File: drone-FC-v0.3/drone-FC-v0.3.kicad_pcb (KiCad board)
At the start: 2 copper layers, 68 parts, among them J1 USB_C_Receptacle_USB2.0_16P, J10 M1, J11 USB_C_Receptacle_USB2.0_16P, J2 Conn_01x04_Pin, J3 S2, J4 S3, J5 S1, J6 Conn_01x04_Pin, J7 ICM, J8 UART0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

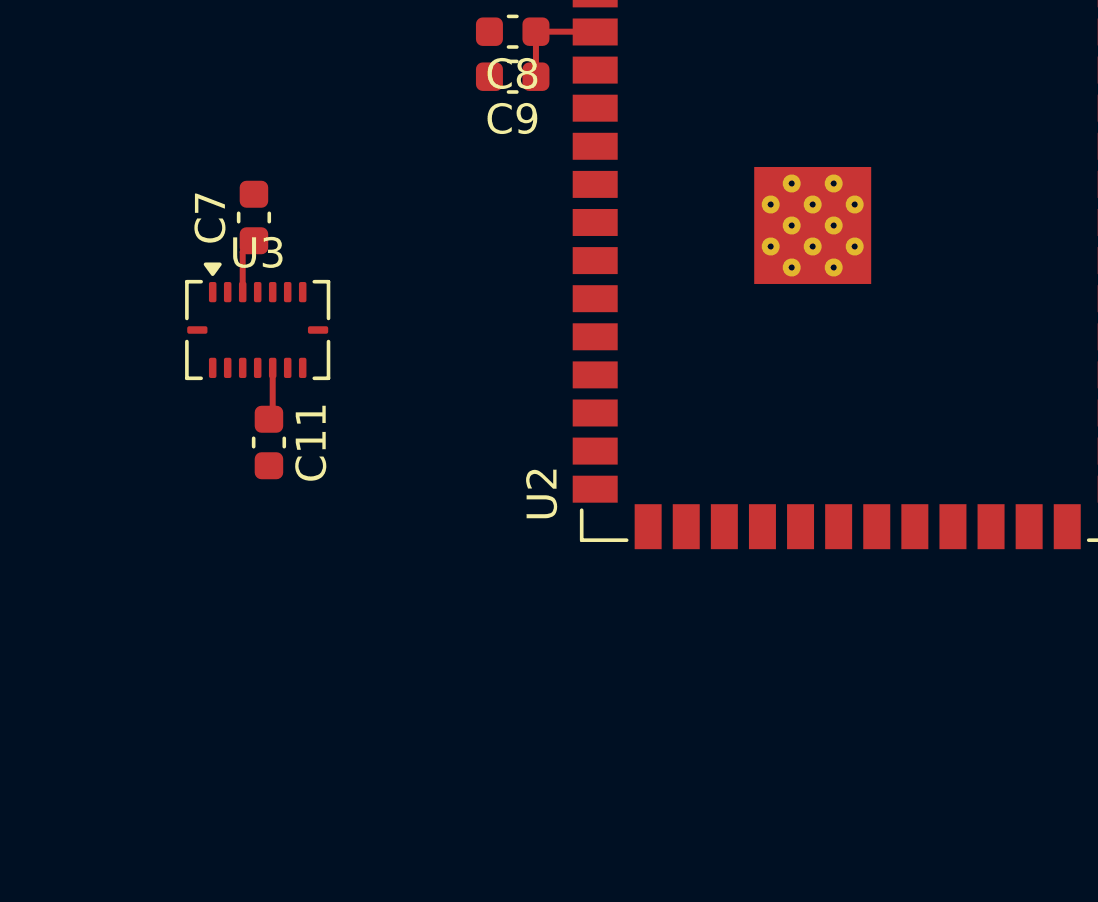
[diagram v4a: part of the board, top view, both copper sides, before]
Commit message: connected U3 to U2
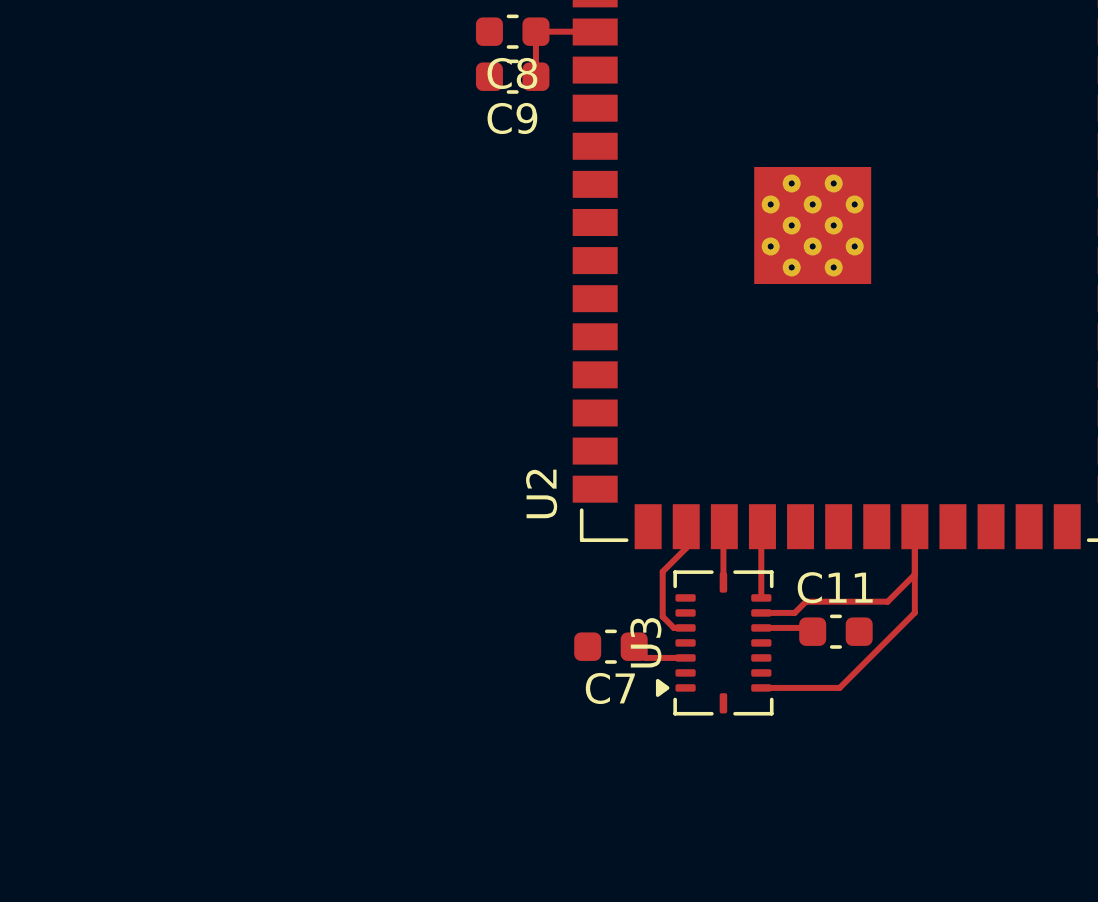
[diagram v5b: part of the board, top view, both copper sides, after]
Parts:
- moved C11 19.9 mm to (137.3, 72.0), turned to 0 degrees
- moved U3 18.7 mm to (133.5, 72.4), turned to 90 degrees
- moved C7 18.6 mm to (129.8, 72.5), turned to 180 degrees
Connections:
- net /Sensors/INT1_ACCEL renamed GPIO4
- net /Sensors/INT2_ACCEL renamed GPIO5
- net /Sensors/INT3_GYRO renamed GPIO6
- net /Sensors/INT4_GYRO renamed GPIO7
- D7 pad 2: /MCU/GPIO 19 -> USB_D-
- D9 pad 2: /MCU/GPIO 20 -> USB_D+
- J10 pad 1: /Power/GPIO8 -> GPIO 8
- J11 pad A6: /MCU/GPIO 20 -> USB_D+
- J11 pad A7: /MCU/GPIO 19 -> USB_D-
- J11 pad B6: /MCU/GPIO 20 -> USB_D+
- J11 pad B7: /MCU/GPIO 19 -> USB_D-
- J2 pad 3: /Sensors/SDA_MAG -> SDA_MAG
- J2 pad 4: /Sensors/SCL_MAG -> SCL_MAG
- J3 pad 1: /Power/GPIO5 -> GPIO 5
- J4 pad 1: /Power/GPIO6 -> GPIO 6
- J5 pad 1: /Power/GPIO4 -> GPIO 4
- J9 pad 1: /Power/GPIO7 -> GPIO 7
- R10 pad 2: /Sensors/SCLK -> SCLK
- R7 pad 2: /Sensors/SCL_MAG -> SCL_MAG
- R8 pad 2: /Sensors/SDA_MAG -> SDA_MAG
- R9 pad 2: /Sensors/GPIO8 -> GPIO 8
- U2 pad 12: /MCU/GPIO8 -> GPIO 8
- U2 pad 13: /MCU/USB_D- -> USB_D-
- U2 pad 14: /MCU/USB_D+ -> USB_D+
- U2 pad 15: /MCU/SCLK -> unconnected-(U2-IO3-Pad15)
- U2 pad 16: unconnected-(U2-IO46-Pad16) -> CSB_GYRO
- U2 pad 17: /MCU/Low_chip_selected -> SCLK
- U2 pad 18: /MCU/SCL_MAG -> MOSI
- U2 pad 19: /MCU/SDA_MAG -> unconnected-(U2-IO11-Pad19)
- U2 pad 20: unconnected-(U2-IO12-Pad20) -> SCL_MAG
- U2 pad 21: unconnected-(U2-IO13-Pad21) -> SDA_MAG
- U2 pad 22: unconnected-(U2-IO14-Pad22) -> MISO
- U2 pad 30: /MCU/SDO1 -> SDO1
- U2 pad 4: /MCU/GPIO4 -> GPIO 4
- U2 pad 5: /MCU/GPIO5 -> GPIO 5
- U2 pad 6: /MCU/GPIO6 -> GPIO 6
- U2 pad 7: /MCU/GPIO7 -> GPIO 7
- U2 pad 8: unconnected-(U2-IO15-Pad8) -> GPIO15
- U3 pad 10: /Sensors/MISO -> MISO
- U3 pad 14: /Sensors/CSB_ACCEL -> GPIO15
- U3 pad 15: /Sensors/MISO -> MISO
- U3 pad 5: /Sensors/CSB_GYRO -> CSB_GYRO
- U3 pad 8: /Sensors/SCK -> SCLK
- U3 pad 9: /Sensors/MOSI -> MOSI
- U6 pad 1: /Sensors/SCL_MAG -> SCL_MAG
- U6 pad 11: /Sensors/SDA_MAG -> SDA_MAG
- U7 pad 7: /Sensors/GPIO8 -> GPIO 8
- U7 pad 8: /Sensors/SCLK -> SCLK
- connector1 pad 2: /Sensors/SDO1 -> SDO1
- connector1 pad 4: /Sensors/SCLK -> SCLK
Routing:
- net MISO: track 0.00 -> 16.3 mm
- net /MCU/GPIO 20: track 9.39 -> 0.00 mm
- net (no net): track 0.00 -> 9.39 mm
- net USB_D-: track 0.00 -> 9.13 mm
- net /MCU/GPIO 19: track 9.13 -> 0.00 mm
- net CSB_GYRO: track 0.00 -> 4.25 mm
- net SCLK: track 0.00 -> 3.90 mm
- net MOSI: track 0.00 -> 2.39 mm
- net GPIO 8: track 0.00 -> 2.04 mm
- net /Sensors/GPIO8: track 2.04 -> 0.00 mm
- net /Sensors/SCLK: track 2.03 -> 0.00 mm
- net SCL_MAG: track 0.00 -> 1.38 mm
- net /Sensors/SCL_MAG: track 1.01 -> 0.00 mm
- net SDA_MAG: track 0.00 -> 0.98 mm
- net /Sensors/SDA_MAG: track 0.98 -> 0.00 mm

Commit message: changed sda and scl labels
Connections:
- R10 pad 2: SCLK -> SCL
- R7 pad 2: SCL_MAG -> SCL
- R8 pad 2: SDA_MAG -> SDA
- R9 pad 2: GPIO 8 -> SDA
- U2 pad 15: unconnected-(U2-IO3-Pad15) -> SCLK
- U2 pad 16: CSB_GYRO -> MOSI
- U2 pad 17: SCLK -> CSB_GYRO
- U2 pad 18: MOSI -> SCL
- U2 pad 19: unconnected-(U2-IO11-Pad19) -> SDA
- U2 pad 20: SCL_MAG -> unconnected-(U2-IO12-Pad20)
- U2 pad 21: SDA_MAG -> unconnected-(U2-IO13-Pad21)
- U2 pad 22: MISO -> unconnected-(U2-IO14-Pad22)
- U2 pad 35: unconnected-(U2-IO42-Pad35) -> MISO
- U6 pad 1: SCL_MAG -> SCL
- U6 pad 11: SDA_MAG -> SDA
- U7 pad 7: GPIO 8 -> SDA
- U7 pad 8: SCLK -> SCL
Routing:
- net SCL: track 0.00 -> 3.04 mm
- net SDA: track 0.00 -> 3.02 mm
- net GPIO 8: track 2.04 -> 0.00 mm
- net SCLK: track 3.90 -> 1.89 mm
- net SCL_MAG: track 1.38 -> 0.00 mm
- net SDA_MAG: track 0.98 -> 0.00 mm
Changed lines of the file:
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@@
 			(size 0.375 0.35)
 			(layers "F.Cu" "F.Mask" "F.Paste")
-			(net "SCL_MAG")
+			(net "SCL")
 			(pinfunction "SCL/SPC_1")
 			(pintype "input")
@@
 			(size 0.375 0.35)
 			(layers "F.Cu" "F.Mask" "F.Paste")
-			(net "SDA_MAG")
+			(net "SDA")
 			(pinfunction "SDA/SDI/SDO_11")
 			(pintype "bidirectional")
@@
 			(layers "F.Cu" "F.Mask" "F.Paste")
 			(roundrect_rratio 0.25)
-			(net "SCLK")
+			(net "SCL")
 			(pintype "passive")
 		)
@@
 			(layers "F.Cu" "F.Mask" "F.Paste")
 			(roundrect_rratio 0.25)
-			(net "SCL_MAG")
+			(net "SCL")
 			(pintype "passive")
 		)
@@
 			(layers "F.Cu" "F.Mask" "F.Paste")
 			(roundrect_rratio 0.25)
-			(net "GPIO 8")
+			(net "SDA")
 			(pintype "passive")
 		)
@@
 				(name "A")
 				(pins "3" "27" "39" "38" "15" "4" "5" "6" "7" "12" "17" "18" "19" "20"
-					"21" "22" "8" "9" "2" "1" "40" "41" "37" "36" "10" "11" "13" "14" "23"
+					"21" "22" "8" "9" "2" "41" "1" "40" "37" "36" "10" "11" "13" "14" "23"
 					"28" "29" "30" "31" "32" "33" "34" "35" "26" "16" "24" "25"
 				)
@@
 			(size 1.5 0.9)
 			(layers "F.Cu" "F.Mask" "F.Paste")
-			(net "unconnected-(U2-IO3-Pad15)")
+			(net "SCLK")
 			(pinfunction "IO3_15")
 			(pintype "bidirectional")
@@
 			(size 1.5 0.9)
 			(layers "F.Cu" "F.Mask" "F.Paste")
-			(net "CSB_GYRO")
+			(net "MOSI")
 			(pinfunction "IO46_16")
 			(pintype "bidirectional")
@@
 			(size 1.5 0.9)
 			(layers "F.Cu" "F.Mask" "F.Paste")
-			(net "SCLK")
+			(net "CSB_GYRO")
 			(pinfunction "IO9_17")
 			(pintype "bidirectional")
@@
 			(size 1.5 0.9)
 			(layers "F.Cu" "F.Mask" "F.Paste")
-			(net "MOSI")
+			(net "SCL")
 			(pinfunction "IO10_18")
 			(pintype "bidirectional")
@@
 			(size 1.5 0.9)
 			(layers "F.Cu" "F.Mask" "F.Paste")
-			(net "unconnected-(U2-IO11-Pad19)")
+			(net "SDA")
 			(pinfunction "IO11_19")
 			(pintype "bidirectional")
@@
 			(size 1.5 0.9)
 			(layers "F.Cu" "F.Mask" "F.Paste")
-			(net "SCL_MAG")
+			(net "unconnected-(U2-IO12-Pad20)")
 			(pinfunction "IO12_20")
 			(pintype "bidirectional")
@@
 			(size 1.5 0.9)
 			(layers "F.Cu" "F.Mask" "F.Paste")
-			(net "SDA_MAG")
+			(net "unconnected-(U2-IO13-Pad21)")
 			(pinfunction "IO13_21")
 			(pintype "bidirectional")
@@
 			(size 1.5 0.9)
 			(layers "F.Cu" "F.Mask" "F.Paste")
-			(net "MISO")
+			(net "unconnected-(U2-IO14-Pad22)")
 			(pinfunction "IO14_22")
 			(pintype "bidirectional")
@@
 			(size 1.5 0.9)
 			(layers "F.Cu" "F.Mask" "F.Paste")
-			(net "unconnected-(U2-IO42-Pad35)")
+			(net "MISO")
 			(pinfunction "IO42_35")
 			(pintype "bidirectional")
@@
 			(layers "F.Cu" "F.Mask" "F.Paste")
 			(roundrect_rratio 0.25)
-			(net "SDA_MAG")
+			(net "SDA")
 			(pintype "passive")
 		)
@@
 			(size 0.95 0.55)
 			(layers "F.Cu" "F.Mask" "F.Paste")
-			(net "GPIO 8")
+			(net "SDA")
 			(pinfunction "SDI/SDA_7")
 			(pintype "bidirectional")
@@
 			(size 0.95 0.55)
 			(layers "F.Cu" "F.Mask" "F.Paste")
-			(net "SCLK")
+			(net "SCL")
 			(pinfunction "SCLK_8")
 			(pintype "input")
@@
 	)
 	(segment
-		(start 150.5 75.5)
-		(end 150.5 76.475)
-		(width 0.2)
-		(layer "F.Cu")
-		(net "SCL_MAG")
-	)
-	(segment
-		(start 137.365 68.865)
-		(end 137.365 68.5)
-		(width 0.2)
-		(layer "F.Cu")
-		(net "SCL_MAG")
-	)
-	(segment
-		(start 150.5 76.475)
-		(end 150.475 76.5)
-		(width 0.2)
-		(layer "F.Cu")
-		(net "SCL_MAG")
-	)
-	(segment
 		(start 110.156 153.506)
 		(end 109.51 153.506)
@@
 	)
 	(segment
-		(start 151.5 76.475)
-		(end 151.4875 76.4875)
-		(width 0.2)
-		(layer "F.Cu")
-		(net "SDA_MAG")
-	)
-	(segment
-		(start 151.5 75.51)
-		(end 151.5 76.475)
-		(width 0.2)
-		(layer "F.Cu")
-		(net "SDA_MAG")
-	)
-	(segment
 		(start 136.5 72)
 		(end 136.375 71.875)
@@
 	)
 	(segment
-		(start 160.0875 55.5)
-		(end 158.0625 55.5)
+		(start 131.025 68.51)
+		(end 131.015 68.5)
 		(width 0.2)
 		(layer "F.Cu")
@@
 	)
 	(segment
-		(start 158.3125 57)
-		(end 158.0625 56.75)
-		(width 0.2)
-		(layer "F.Cu")
-		(net "GPIO 8")
-	)
-	(segment
-		(start 160 57)
-		(end 158.3125 57)
-		(width 0.2)
-		(layer "F.Cu")
-		(net "GPIO 8")
-	)
-	(segment
 		(start 231.45 25.675)
 		(end 231.7 25.925)
@@
 	)
 	(segment
+		(start 131.875 71.875)
+		(end 131.5 71.5)
+		(width 0.2)
+		(layer "F.Cu")
+		(net "CSB_GYRO")
+	)
+	(segment
+		(start 132.2625 71.875)
+		(end 131.875 71.875)
+		(width 0.2)
+		(layer "F.Cu")
+		(net "CSB_GYRO")
+	)
+	(segment
+		(start 132.2875 68.5025)
+		(end 132.285 68.5)
+		(width 0.2)
+		(layer "F.Cu")
+		(net "CSB_GYRO")
+	)
+	(segment
+		(start 131.5 71.5)
+		(end 131.5 70)
+		(width 0.2)
+		(layer "F.Cu")
+		(net "CSB_GYRO")
+	)
+	(segment
+		(start 131.5 70)
+		(end 132.285 69.215)
+		(width 0.2)
+		(layer "F.Cu")
+		(net "CSB_GYRO")
+	)
+	(segment
+		(start 132.285 69.215)
+		(end 132.285 68.5)
+		(width 0.2)
+		(layer "F.Cu")
+		(net "CSB_GYRO")
+	)
+	(segment
 		(start 134.7875 68.5375)
 		(end 134.825 68.5)
@@
 	)
 	(segment
-		(start 131.875 71.875)
-		(end 131.5 71.5)
+		(start 129.15 61)
+		(end 129.25 60.9)
 		(width 0.2)
 		(layer "F.Cu")
-		(net "CSB_GYRO")
+		(net "unconnected-(U2-IO16-Pad9)")
 	)
 	(segment
-		(start 132.2625 71.875)
-		(end 131.875 71.875)
+		(start 150.5 75.5)
+		(end 150.5 76.475)
 		(width 0.2)
 		(layer "F.Cu")
-		(net "CSB_GYRO")
+		(net "SCL")
 	)
 	(segment
-		(start 132.2875 68.5025)
-		(end 132.285 68.5)
+		(start 150.5 76.475)
+		(end 150.475 76.5)
 		(width 0.2)
 		(layer "F.Cu")
-		(net "CSB_GYRO")
+		(net "SCL")
 	)
 	(segment
-		(start 131.5 71.5)
-		(end 131.5 70)
+		(start 160.0875 55.5)
+		(end 158.0625 55.5)
 		(width 0.2)
 		(layer "F.Cu")
-		(net "CSB_GYRO")
+		(net "SCL")
 	)
 	(segment
-		(start 131.5 70)
-		(end 132.285 69.215)
+		(start 151.5 76.475)
+		(end 151.4875 76.4875)
 		(width 0.2)
 		(layer "F.Cu")
-		(net "CSB_GYRO")
+		(net "SDA")
 	)
 	(segment
-		(start 132.285 69.215)
-		(end 132.285 68.5)
+		(start 151.5 75.51)
+		(end 151.5 76.475)
 		(width 0.2)
 		(layer "F.Cu")
-		(net "CSB_GYRO")
+		(net "SDA")
 	)
 	(segment
-		(start 131.025 68.51)
-		(end 131.015 68.5)
+		(start 158.3125 57)
+		(end 158.0625 56.75)
 		(width 0.2)
 		(layer "F.Cu")
-		(net "unconnected-(U2-IO3-Pad15)")
+		(net "SDA")
 	)
 	(segment
-		(start 129.15 61)
-		(end 129.25 60.9)
+		(start 160 57)
+		(end 158.3125 57)
 		(width 0.2)
 		(layer "F.Cu")
-		(net "unconnected-(U2-IO16-Pad9)")
+		(net "SDA")
+	)
+	(segment
+		(start 137.365 68.865)
+		(end 137.365 68.5)
+		(width 0.2)
+		(layer "F.Cu")
+		(net "unconnected-(U2-IO12-Pad20)")
 	)
 	(embedded_fonts no)
